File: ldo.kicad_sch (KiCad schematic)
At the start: 5 parts, among them U301 MIC37100-3.3WS-TR

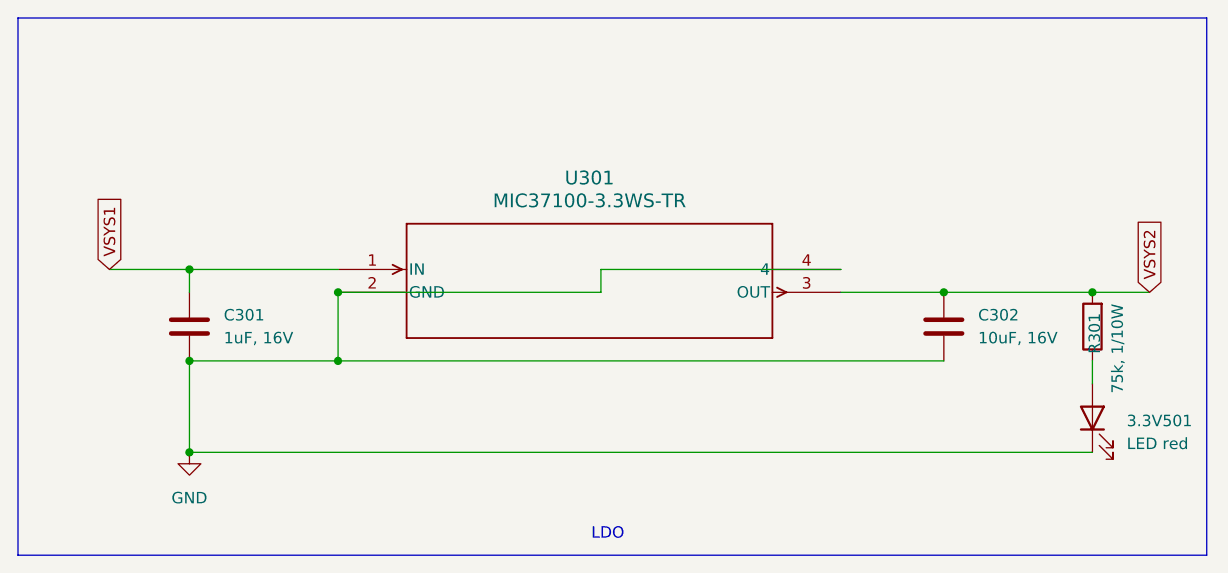
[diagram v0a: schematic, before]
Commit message: daughterboard created
divided into mainboard and daughterboard
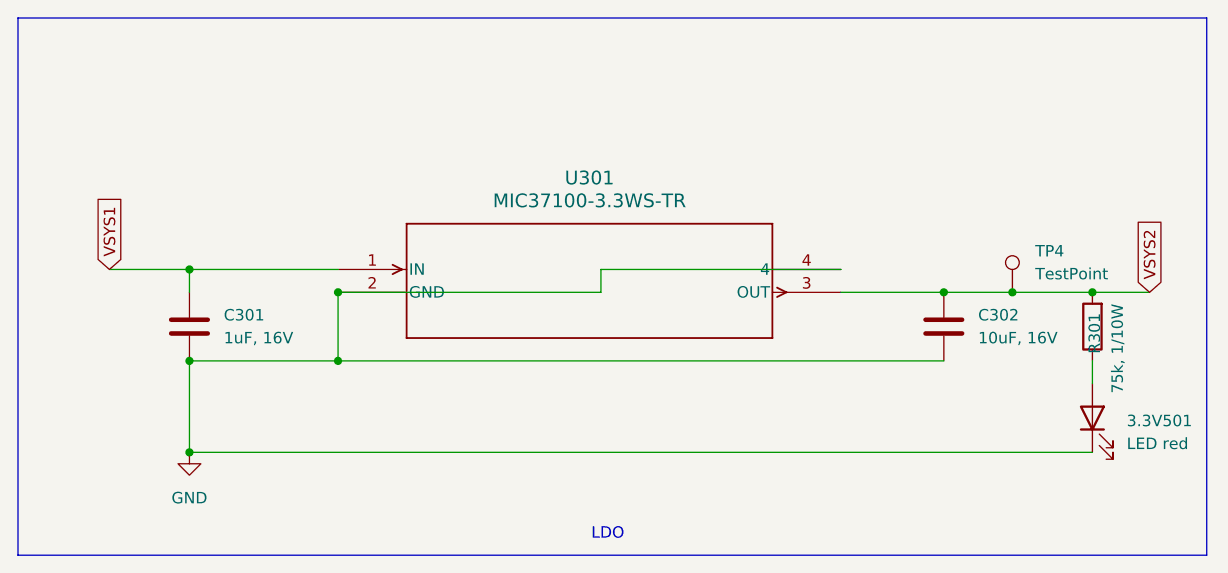
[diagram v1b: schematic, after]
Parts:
- added TP4: TestPoint, TestPoint:TestPoint_Pad_D1.0mm, symbol Connector:TestPoint
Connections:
- net VSYS2: now also TP4.1
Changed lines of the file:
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@@
 		(color 0 0 0 0)
 	)
+	(junction
+		(at 133.35 53.34)
+		(diameter 0)
+		(color 0 0 0 0)
+	)
 	(wire
 		(pts
@@
 	(wire
 		(pts
+			(xy 133.35 53.34) (xy 142.24 53.34)
+		)
+		(stroke
+			(width 0)
+			(type default)
+		)
+	)
+	(wire
+		(pts
 			(xy 87.63 50.8) (xy 87.63 53.34)
 		)
@@
 	(wire
 		(pts
-			(xy 125.73 53.34) (xy 142.24 53.34)
+			(xy 125.73 53.34) (xy 133.35 53.34)
 		)
 		(stroke
@@
 					(unit 1)
 				)
+			)
+		)
+	)
+	(symbol
+		(lib_id "Connector:TestPoint")
+		(at 133.35 53.34 0)
+		(unit 1)
+		(exclude_from_sim no)
+		(in_bom yes)
+		(on_board yes)
+		(dnp no)
+		(fields_autoplaced yes)
+		(property "Reference" "TP4"
+			(at 135.89 48.7679 0)
+			(effects
+				(font
+					(size 1.27 1.27)
+				)
+				(justify left)
+			)
+		)
+		(property "Value" "TestPoint"
+			(at 135.89 51.3079 0)
+			(effects
+				(font
+					(size 1.27 1.27)
+				)
+				(justify left)
+			)
+		)
+		(property "Footprint" "TestPoint:TestPoint_Pad_D1.0mm"
+			(at 138.43 53.34 0)
+			(effects
+				(font
+					(size 1.27 1.27)
+				)
+				(hide yes)
+			)
+		)
+		(property "Datasheet" "~"
+			(at 138.43 53.34 0)
+			(effects
+				(font
+					(size 1.27 1.27)
+				)
+				(hide yes)
+			)
+		)
+		(property "Description" "test point"
+			(at 133.35 53.34 0)
+			(effects
+				(font
+					(size 1.27 1.27)
+				)
+				(hide yes)
+			)
+		)
+		(pin "1"
+		)
+		(instances
+			(project ""
+				(path "/63d8ebc3-d81d-4869-925f-b28ad884a523/85811e20-2610-48e4-a5bf-8edeeb1afe1f"
+					(reference "TP4")
+					(unit 1)
+				)
